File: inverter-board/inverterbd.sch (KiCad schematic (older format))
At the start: 14 parts, among them J1 Conn_01x03, J2 Conn_01x03, J3 Conn_01x03, J4 Conn_01x03, J5 Conn_01x03, Q1 2N7000, Q2 2N7000, Q3 2N7000, Q4 2N7000

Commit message: fixed MOSFET polarity
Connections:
- net Earth: now also Q1.1 (S), Q2.1 (S), Q3.1 (S), Q4.1 (S); no longer Q1.3 (D), Q2.3 (D), Q3.3 (D), Q4.3 (D)
- net signal: now also Q1.3 (D), Q2.3 (D), Q3.3 (D), Q4.3 (D); no longer Q1.1 (S), Q2.1 (S), Q3.1 (S), Q4.1 (S)
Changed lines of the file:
@@
 F 3 "https://www.fairchildsemi.com/datasheets/2N/2N7000.pdf" H 7250 2750 50  0001 L CNN
 	1    7250 2750
-	-1   0    0    1
+	-1   0    0    -1
 $EndComp
 Wire Wire Line
@@
 F 3 "https://www.fairchildsemi.com/datasheets/2N/2N7000.pdf" H 7250 3350 50  0001 L CNN
 	1    7250 3350
-	-1   0    0    1
+	-1   0    0    -1
 $EndComp
 Wire Wire Line
@@
 F 3 "https://www.fairchildsemi.com/datasheets/2N/2N7000.pdf" H 7250 3950 50  0001 L CNN
 	1    7250 3950
-	-1   0    0    1
+	-1   0    0    -1
 $EndComp
 Wire Wire Line
@@
 F 3 "https://www.fairchildsemi.com/datasheets/2N/2N7000.pdf" H 7250 4550 50  0001 L CNN
 	1    7250 4550
-	-1   0    0    1
+	-1   0    0    -1
 $EndComp
 Wire Wire Line

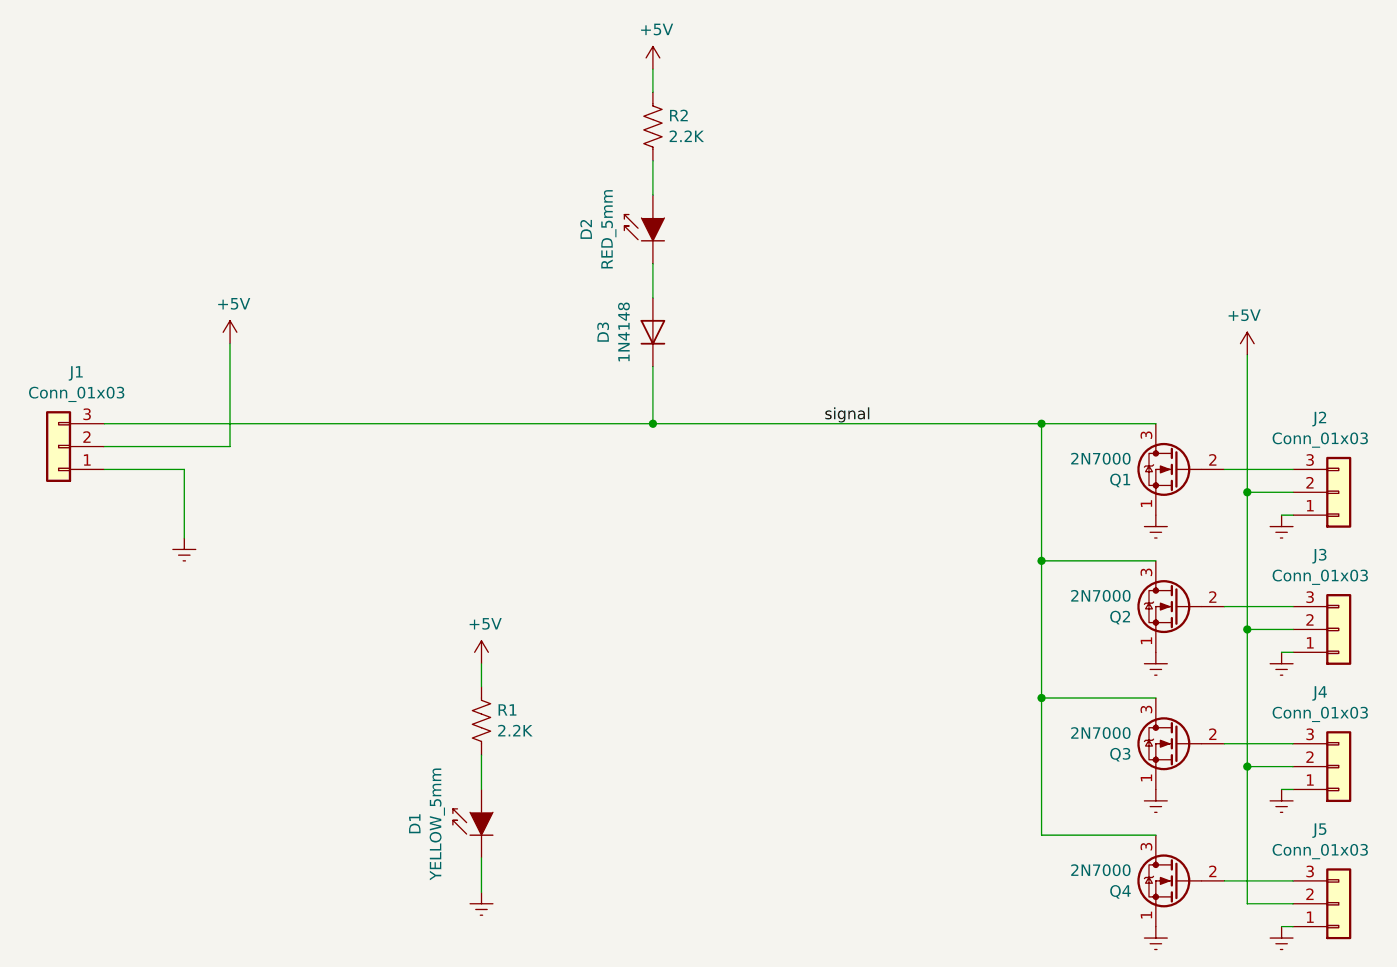
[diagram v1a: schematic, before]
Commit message: added pulldown resistors
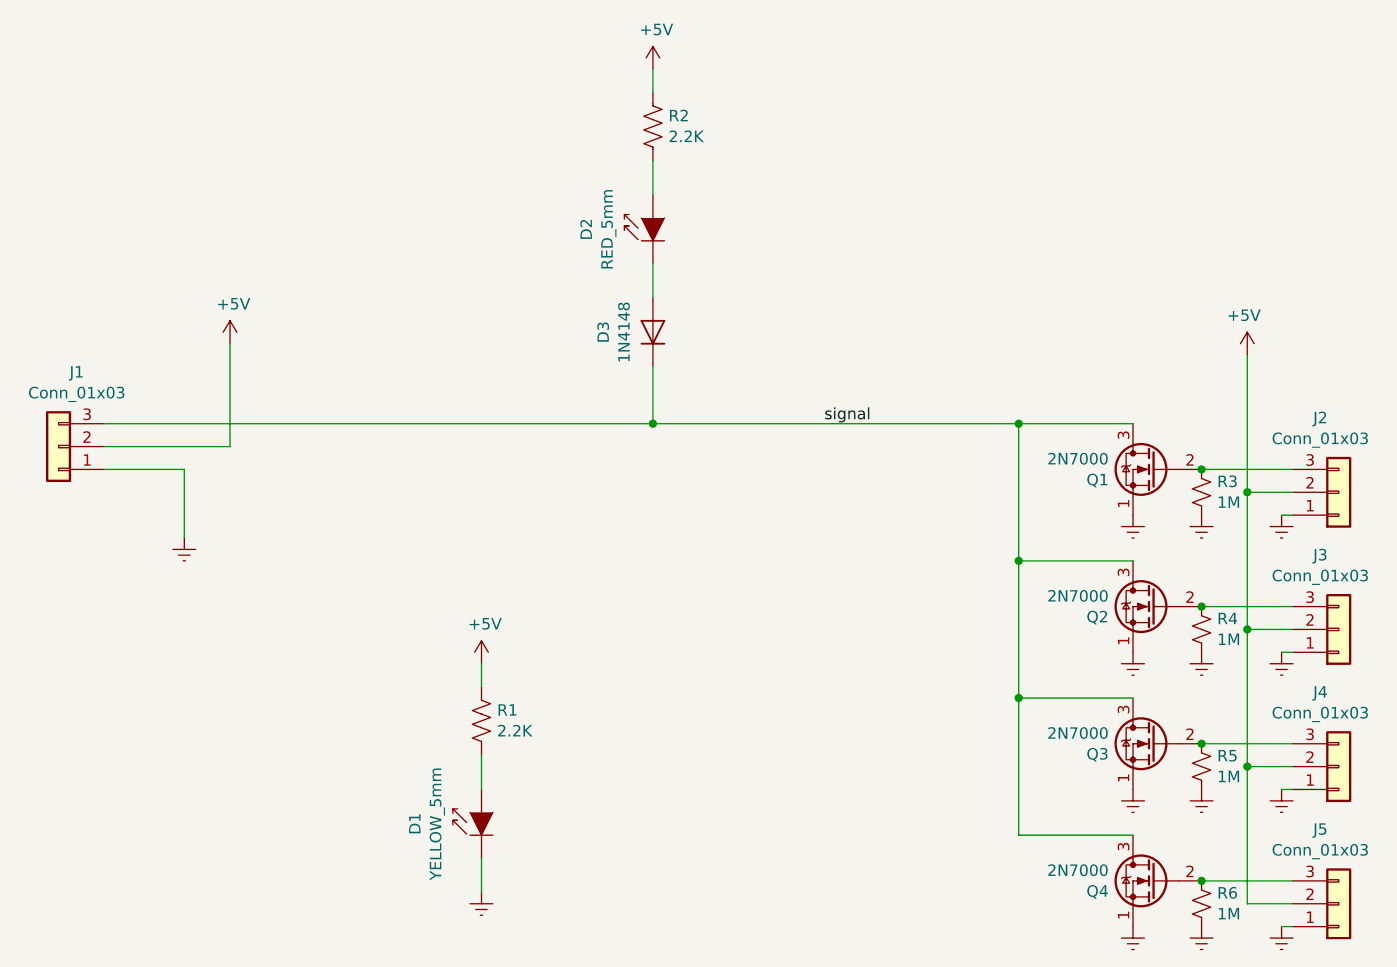
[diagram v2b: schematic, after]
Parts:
- added R3, R4, R5, R6: 1M, Resistor_THT:R_Axial_DIN0207_L6.3mm_D2.5mm_P10.16mm_Horizontal, symbol Device:R_Small_US
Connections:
- net Earth: now also R3.2, R4.2, R5.2, R6.2
- net at J2.3 (Pin_3), Q1.2 (G): now also R3.1
- net at J3.3 (Pin_3), Q2.2 (G): now also R4.1
- net at J4.3 (Pin_3), Q3.2 (G): now also R5.1
- net at J5.3 (Pin_3), Q4.2 (G): now also R6.1
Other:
- moved on the sheet: Q1, Q2, Q3, Q4
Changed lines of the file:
@@
 $EndComp
-Wire Wire Line
-	2550 2550 4950 2550
 Wire Wire Line
 	4950 1850 4950 2000
@@
 L Transistor_FET:2N7000 Q1
 U 1 1 5C730356
-P 7250 2750
-F 0 "Q1" H 7456 2704 50  0000 L CNN
-F 1 "2N7000" H 7456 2795 50  0000 L CNN
-F 2 "Package_TO_SOT_THT:TO-92_Inline" H 7450 2675 50  0001 L CIN
-F 3 "https://www.fairchildsemi.com/datasheets/2N/2N7000.pdf" H 7250 2750 50  0001 L CNN
-	1    7250 2750
-	-1   0    0    -1
-$EndComp
-Wire Wire Line
-	7750 2750 7450 2750
+P 7150 2750
+F 0 "Q1" H 7356 2704 50  0000 L CNN
+F 1 "2N7000" H 7356 2795 50  0000 L CNN
+F 2 "Package_TO_SOT_THT:TO-92_Inline" H 7350 2675 50  0001 L CIN
+F 3 "https://www.fairchildsemi.com/datasheets/2N/2N7000.pdf" H 7150 2750 50  0001 L CNN
+	1    7150 2750
+	-1   0    0    -1
+$EndComp
 Wire Wire Line
 	7550 2850 7750 2850
 Wire Wire Line
 	7550 2250 7550 2850
-Wire Wire Line
-	4950 2550 6650 2550
 $Comp
 L power:Earth #PWR0108
 U 1 1 5C735E8D
-P 7150 2950
-F 0 "#PWR0108" H 7150 2700 50  0001 C CNN
-F 1 "Earth" H 7150 2800 50  0001 C CNN
-F 2 "" H 7150 2950 50  0001 C CNN
-F 3 "~" H 7150 2950 50  0001 C CNN
-	1    7150 2950
+P 7050 2950
+F 0 "#PWR0108" H 7050 2700 50  0001 C CNN
+F 1 "Earth" H 7050 2800 50  0001 C CNN
+F 2 "" H 7050 2950 50  0001 C CNN
+F 3 "~" H 7050 2950 50  0001 C CNN
+	1    7050 2950
 	-1   0    0    -1
 $EndComp
@@
 L Transistor_FET:2N7000 Q2
 U 1 1 5C737452
-P 7250 3350
-F 0 "Q2" H 7456 3304 50  0000 L CNN
-F 1 "2N7000" H 7456 3395 50  0000 L CNN
-F 2 "Package_TO_SOT_THT:TO-92_Inline" H 7450 3275 50  0001 L CIN
-F 3 "https://www.fairchildsemi.com/datasheets/2N/2N7000.pdf" H 7250 3350 50  0001 L CNN
-	1    7250 3350
-	-1   0    0    -1
-$EndComp
-Wire Wire Line
-	7750 3350 7450 3350
+P 7150 3350
+F 0 "Q2" H 7356 3304 50  0000 L CNN
+F 1 "2N7000" H 7356 3395 50  0000 L CNN
+F 2 "Package_TO_SOT_THT:TO-92_Inline" H 7350 3275 50  0001 L CIN
+F 3 "https://www.fairchildsemi.com/datasheets/2N/2N7000.pdf" H 7150 3350 50  0001 L CNN
+	1    7150 3350
+	-1   0    0    -1
+$EndComp
 Wire Wire Line
 	7550 3450 7750 3450
@@
 L power:Earth #PWR0110
 U 1 1 5C73745B
-P 7150 3550
-F 0 "#PWR0110" H 7150 3300 50  0001 C CNN
-F 1 "Earth" H 7150 3400 50  0001 C CNN
-F 2 "" H 7150 3550 50  0001 C CNN
-F 3 "~" H 7150 3550 50  0001 C CNN
-	1    7150 3550
+P 7050 3550
+F 0 "#PWR0110" H 7050 3300 50  0001 C CNN
+F 1 "Earth" H 7050 3400 50  0001 C CNN
+F 2 "" H 7050 3550 50  0001 C CNN
+F 3 "~" H 7050 3550 50  0001 C CNN
+	1    7050 3550
 	-1   0    0    -1
 $EndComp
@@
 L Transistor_FET:2N7000 Q3
 U 1 1 5C73776E
-P 7250 3950
-F 0 "Q3" H 7456 3904 50  0000 L CNN
-F 1 "2N7000" H 7456 3995 50  0000 L CNN
-F 2 "Package_TO_SOT_THT:TO-92_Inline" H 7450 3875 50  0001 L CIN
-F 3 "https://www.fairchildsemi.com/datasheets/2N/2N7000.pdf" H 7250 3950 50  0001 L CNN
-	1    7250 3950
-	-1   0    0    -1
-$EndComp
-Wire Wire Line
-	7750 3950 7450 3950
+P 7150 3950
+F 0 "Q3" H 7356 3904 50  0000 L CNN
+F 1 "2N7000" H 7356 3995 50  0000 L CNN
+F 2 "Package_TO_SOT_THT:TO-92_Inline" H 7350 3875 50  0001 L CIN
+F 3 "https://www.fairchildsemi.com/datasheets/2N/2N7000.pdf" H 7150 3950 50  0001 L CNN
+	1    7150 3950
+	-1   0    0    -1
+$EndComp
 Wire Wire Line
 	7550 4050 7750 4050
@@
 L power:Earth #PWR0112
 U 1 1 5C737777
-P 7150 4150
-F 0 "#PWR0112" H 7150 3900 50  0001 C CNN
-F 1 "Earth" H 7150 4000 50  0001 C CNN
-F 2 "" H 7150 4150 50  0001 C CNN
-F 3 "~" H 7150 4150 50  0001 C CNN
-	1    7150 4150
+P 7050 4150
+F 0 "#PWR0112" H 7050 3900 50  0001 C CNN
+F 1 "Earth" H 7050 4000 50  0001 C CNN
+F 2 "" H 7050 4150 50  0001 C CNN
+F 3 "~" H 7050 4150 50  0001 C CNN
+	1    7050 4150
 	-1   0    0    -1
 $EndComp
@@
 L Transistor_FET:2N7000 Q4
 U 1 1 5C737D2D
-P 7250 4550
-F 0 "Q4" H 7456 4504 50  0000 L CNN
-F 1 "2N7000" H 7456 4595 50  0000 L CNN
-F 2 "Package_TO_SOT_THT:TO-92_Inline" H 7450 4475 50  0001 L CIN
-F 3 "https://www.fairchildsemi.com/datasheets/2N/2N7000.pdf" H 7250 4550 50  0001 L CNN
-	1    7250 4550
-	-1   0    0    -1
-$EndComp
-Wire Wire Line
-	7750 4550 7450 4550
+P 7150 4550
+F 0 "Q4" H 7356 4504 50  0000 L CNN
+F 1 "2N7000" H 7356 4595 50  0000 L CNN
+F 2 "Package_TO_SOT_THT:TO-92_Inline" H 7350 4475 50  0001 L CIN
+F 3 "https://www.fairchildsemi.com/datasheets/2N/2N7000.pdf" H 7150 4550 50  0001 L CNN
+	1    7150 4550
+	-1   0    0    -1
+$EndComp
 Wire Wire Line
 	7550 4650 7750 4650
@@
 L power:Earth #PWR0114
 U 1 1 5C737D36
-P 7150 4750
-F 0 "#PWR0114" H 7150 4500 50  0001 C CNN
-F 1 "Earth" H 7150 4600 50  0001 C CNN
-F 2 "" H 7150 4750 50  0001 C CNN
-F 3 "~" H 7150 4750 50  0001 C CNN
-	1    7150 4750
+P 7050 4750
+F 0 "#PWR0114" H 7050 4500 50  0001 C CNN
+F 1 "Earth" H 7050 4600 50  0001 C CNN
+F 2 "" H 7050 4750 50  0001 C CNN
+F 3 "~" H 7050 4750 50  0001 C CNN
+	1    7050 4750
 	-1   0    0    -1
 $EndComp
@@
 Connection ~ 7550 4050
 Wire Wire Line
-	7150 3150 6650 3150
-Wire Wire Line
-	6650 3150 6650 2550
-Connection ~ 6650 2550
-Wire Wire Line
-	6650 2550 7150 2550
-Wire Wire Line
-	7150 3750 6650 3750
-Wire Wire Line
-	6650 3750 6650 3150
-Connection ~ 6650 3150
-Wire Wire Line
-	7150 4350 6650 4350
-Wire Wire Line
-	6650 4350 6650 3750
-Connection ~ 6650 3750
+	7050 3150 6550 3150
+Wire Wire Line
+	6550 3150 6550 2550
+Connection ~ 6550 2550
+Wire Wire Line
+	6550 2550 7050 2550
+Wire Wire Line
+	7050 3750 6550 3750
+Wire Wire Line
+	6550 3750 6550 3150
+Connection ~ 6550 3150
+Wire Wire Line
+	7050 4350 6550 4350
+Wire Wire Line
+	6550 4350 6550 3750
+Connection ~ 6550 3750
+$Comp
+L Device:R_Small_US R6
+U 1 1 5C7482B1
+P 7350 4650
+F 0 "R6" H 7418 4696 50  0000 L CNN
+F 1 "1M" H 7418 4605 50  0000 L CNN
+F 2 "Resistor_THT:R_Axial_DIN0207_L6.3mm_D2.5mm_P10.16mm_Horizontal" H 7350 4650 50  0001 C CNN
+F 3 "~" H 7350 4650 50  0001 C CNN
+	1    7350 4650
+	1    0    0    -1
+$EndComp
+$Comp
+L power:Earth #PWR04
+U 1 1 5C748373
+P 7350 4750
+F 0 "#PWR04" H 7350 4500 50  0001 C CNN
+F 1 "Earth" H 7350 4600 50  0001 C CNN
+F 2 "" H 7350 4750 50  0001 C CNN
+F 3 "~" H 7350 4750 50  0001 C CNN
+	1    7350 4750
+	-1   0    0    -1
+$EndComp
+Wire Wire Line
+	4950 2550 6550 2550
+Wire Wire Line
+	2550 2550 4950 2550
+Wire Wire Line
+	7350 4550 7750 4550
+Wire Wire Line
+	7350 3950 7750 3950
+Wire Wire Line
+	7350 3350 7750 3350
+Wire Wire Line
+	7350 2750 7750 2750
+Connection ~ 7350 4550
+$Comp
+L Device:R_Small_US R3
+U 1 1 5C74C770
+P 7350 2850
+F 0 "R3" H 7418 2896 50  0000 L CNN
+F 1 "1M" H 7418 2805 50  0000 L CNN
+F 2 "Resistor_THT:R_Axial_DIN0207_L6.3mm_D2.5mm_P10.16mm_Horizontal" H 7350 2850 50  0001 C CNN
+F 3 "~" H 7350 2850 50  0001 C CNN
+	1    7350 2850
+	1    0    0    -1
+$EndComp
+$Comp
+L power:Earth #PWR01
+U 1 1 5C74C7CA
+P 7350 2950
+F 0 "#PWR01" H 7350 2700 50  0001 C CNN
+F 1 "Earth" H 7350 2800 50  0001 C CNN
+F 2 "" H 7350 2950 50  0001 C CNN
+F 3 "~" H 7350 2950 50  0001 C CNN
+	1    7350 2950
+	-1   0    0    -1
+$EndComp
+$Comp
+L Device:R_Small_US R5
+U 1 1 5C74C854
+P 7350 4050
+F 0 "R5" H 7418 4096 50  0000 L CNN
+F 1 "1M" H 7418 4005 50  0000 L CNN
+F 2 "Resistor_THT:R_Axial_DIN0207_L6.3mm_D2.5mm_P10.16mm_Horizontal" H 7350 4050 50  0001 C CNN
+F 3 "~" H 7350 4050 50  0001 C CNN
+	1    7350 4050
+	1    0    0    -1
+$EndComp
+$Comp
+L power:Earth #PWR03
+U 1 1 5C74C85A
+P 7350 4150
+F 0 "#PWR03" H 7350 3900 50  0001 C CNN
+F 1 "Earth" H 7350 4000 50  0001 C CNN
+F 2 "" H 7350 4150 50  0001 C CNN
+F 3 "~" H 7350 4150 50  0001 C CNN
+	1    7350 4150
+	-1   0    0    -1
+$EndComp
+Connection ~ 7350 3950
+$Comp
+L Device:R_Small_US R4
+U 1 1 5C74CDD6
+P 7350 3450
+F 0 "R4" H 7418 3496 50  0000 L CNN
+F 1 "1M" H 7418 3405 50  0000 L CNN
+F 2 "Resistor_THT:R_Axial_DIN0207_L6.3mm_D2.5mm_P10.16mm_Horizontal" H 7350 3450 50  0001 C CNN
+F 3 "~" H 7350 3450 50  0001 C CNN
+	1    7350 3450
+	1    0    0    -1
+$EndComp
+$Comp
+L power:Earth #PWR02
+U 1 1 5C74CDDC
+P 7350 3550
+F 0 "#PWR02" H 7350 3300 50  0001 C CNN
+F 1 "Earth" H 7350 3400 50  0001 C CNN
+F 2 "" H 7350 3550 50  0001 C CNN
+F 3 "~" H 7350 3550 50  0001 C CNN
+	1    7350 3550
+	-1   0    0    -1
+$EndComp
+Connection ~ 7350 3350
+Connection ~ 7350 2750
 $EndSCHEMATC
